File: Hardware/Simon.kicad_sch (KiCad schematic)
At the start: 7 parts

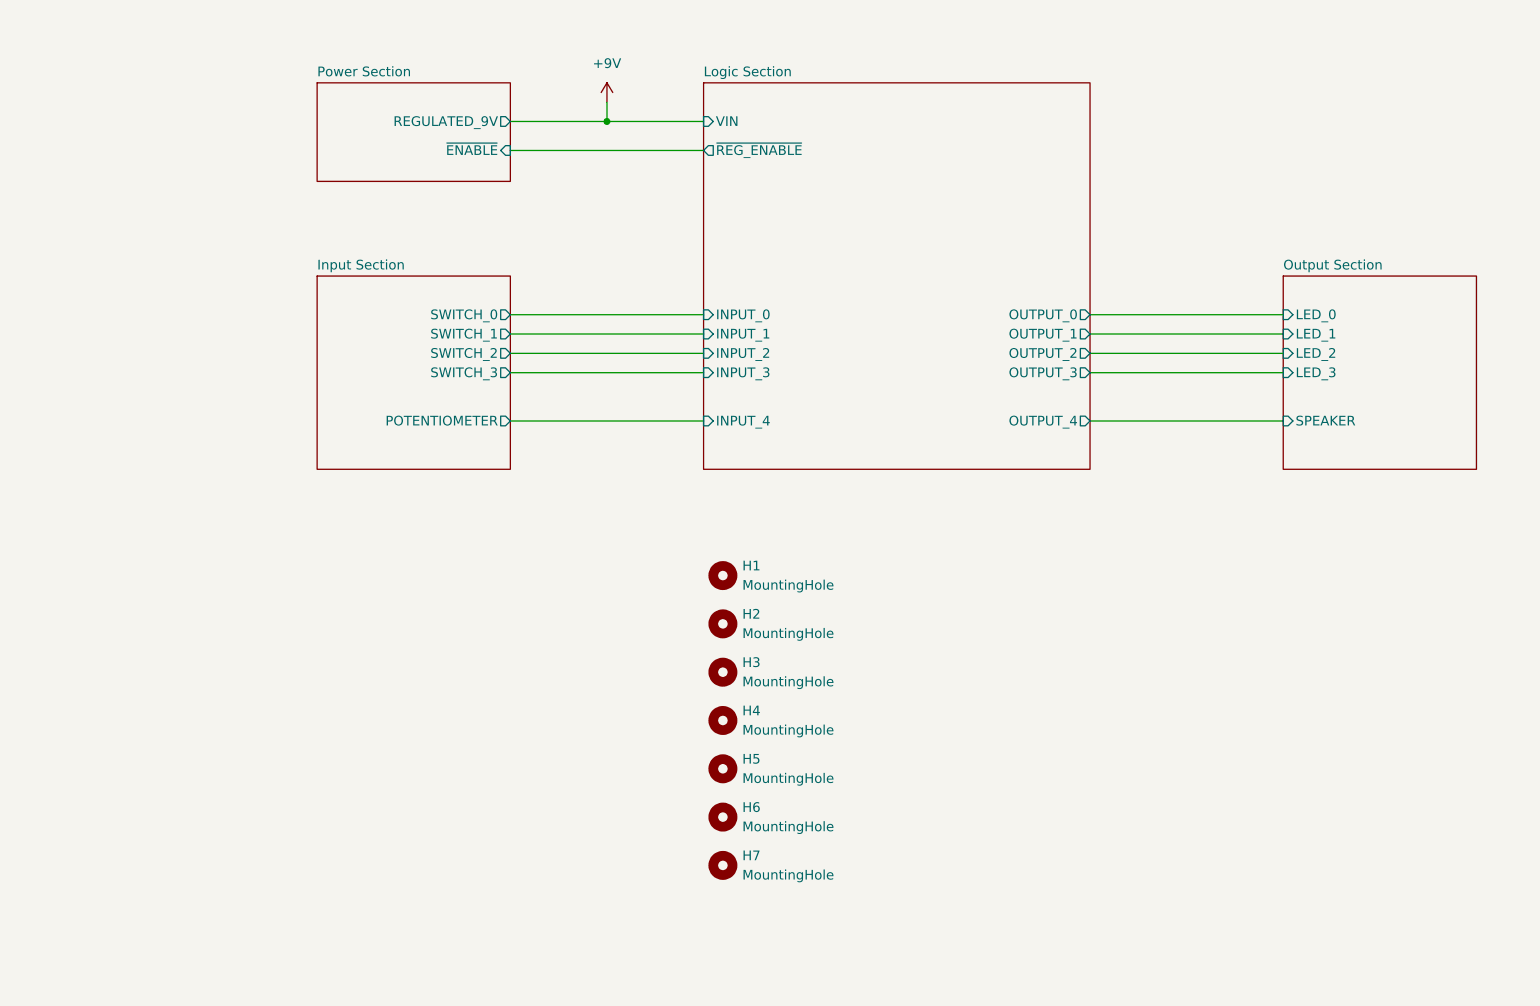
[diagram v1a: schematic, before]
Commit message: Updated KiCAD project.
- Added grouping in schematics.
- Removed unnecessary net names in "LogicSection.kicad_sch".
- Added 330R between +5V and nREG_ENABLE.
- Changed path for 3D models.
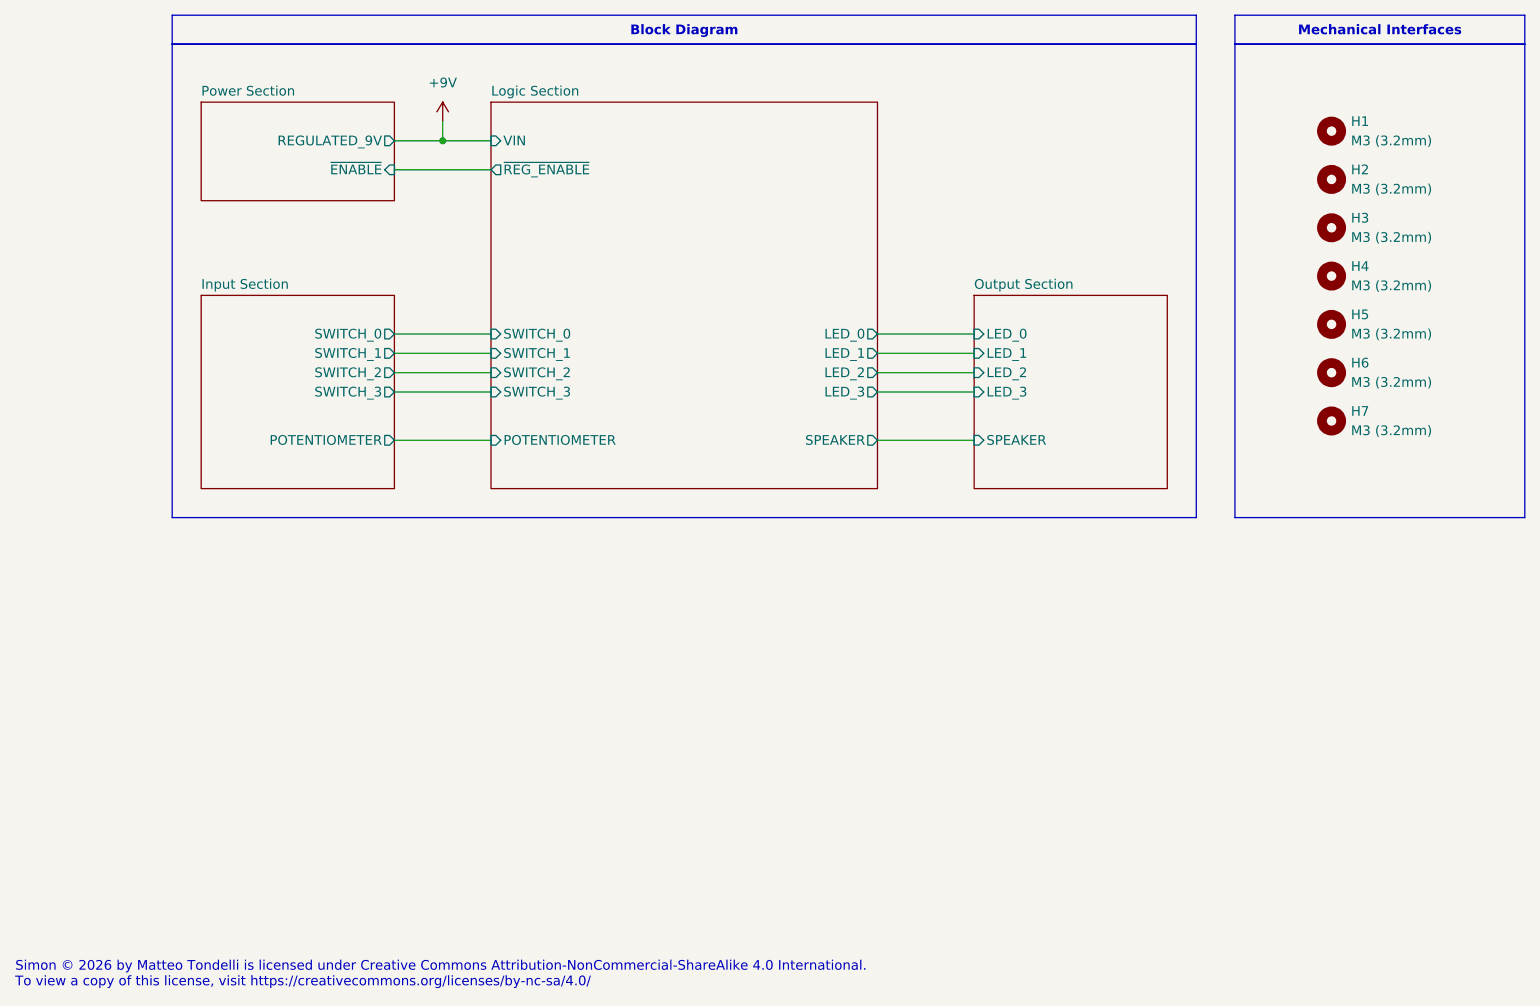
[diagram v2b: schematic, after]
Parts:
- H1, H2, H3, H4, H5, H6, H7: value MountingHole -> M3 (3.2mm)
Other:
- sheet Logic Section ports: added LED_0, LED_1, LED_2, LED_3, POTENTIOMETER, SPEAKER, SWITCH_0, SWITCH_1, SWITCH_2, SWITCH_3; removed INPUT_0, INPUT_1, INPUT_2, INPUT_3, INPUT_4, OUTPUT_0, OUTPUT_1, OUTPUT_2, OUTPUT_3, OUTPUT_4
- moved on the sheet: H1, H2, H3, H4, H5, H6, H7
